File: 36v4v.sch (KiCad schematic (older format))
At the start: 38 parts, among them J1 Conn_01x03, J2 Conn_01x02, J3 Conn_01x02, J4 Conn_01x02, J5 Conn_01x02, U1 InnoSwitch3-CE, INN3162C, inS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

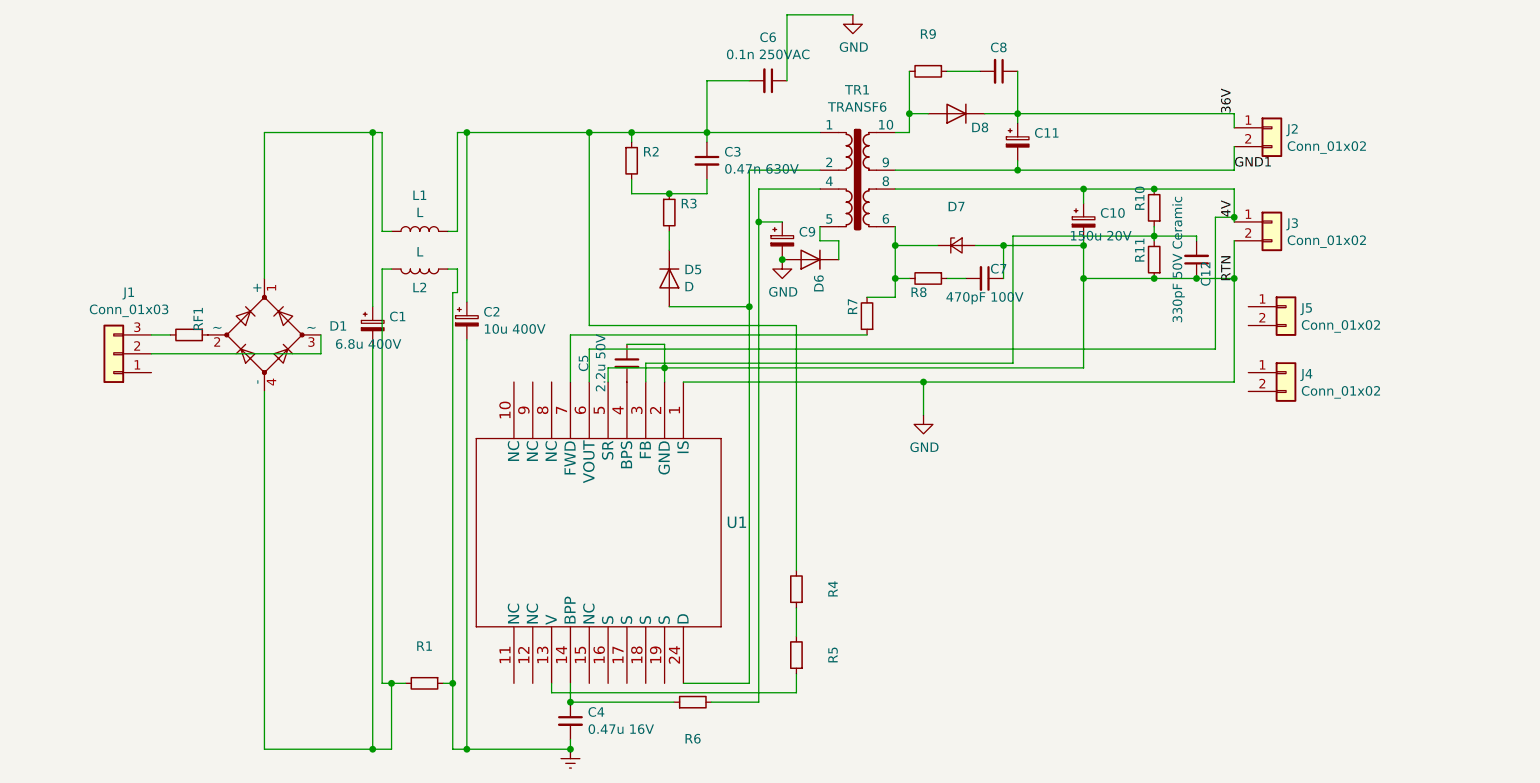
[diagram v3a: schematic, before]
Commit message: Changes to components and footprints as suggested by AA
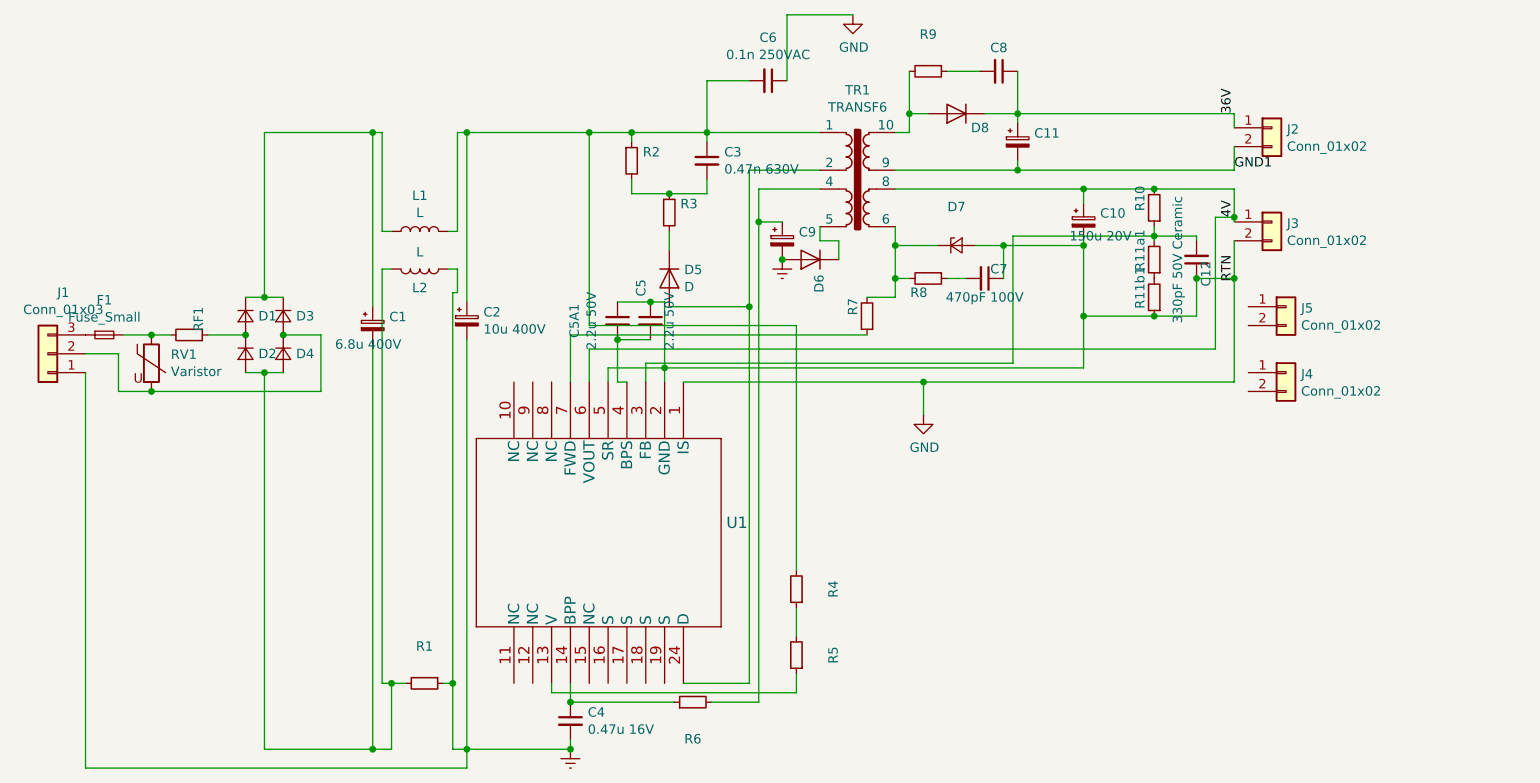
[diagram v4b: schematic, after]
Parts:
- removed D1: D_Bridge_+AA- / 800 V, 1 A, Standard Recovery, DO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, Diode_THT:Diode_Bridge_Vishay_GBL, symbol Device:D_Bridge_+AA-
- added C5A1: 2.2u 50V, Capacitor_SMD:C_0603_1608Metric_Pad1.05x0.95mm_HandSolder, symbol Device:C_Small
- added D1, D2, D3, D4: D_Small, Diode_SMD:D_SMB_Handsoldering, symbol Device:D_Small
- added F1: Fuse_Small, Fuse:Fuse_0805_2012Metric, symbol Device:Fuse_Small
- added R11b1: 29.4 kΩ, 1 %, 0.125 W, Metal Film, Resistor_SMD:R_0603_1608Metric_Pad1.05x0.95mm_HandSolder, symbol Device:R_Small
- added RV1: Varistor, Varistor:RV_Disc_D7mm_W4mm_P5mm, symbol Device:Varistor
- C1, C2: footprint pwrcon:CP_Elec_EEV_16x17.5 -> Capacitor_THT:CP_Radial_D10.0mm_P5.00mm; MFG Name Panasonic -> Kemet/Panasonic; MFG Part Num EEV-EB2G100SM -> ESH106M450AH4AA/EEV-EB2G100SM
- C10: MFG Name Nichikon -> Nichikon/Wurth; MFG Part Num PLF1D151MDO2TD -> PLF1D151MDO2TD/860010674014
- C11: MFG Name United Chemi-Con -> Wurth/United Chemi-Con; MFG Part Num EKZE500ELL220ME11D -> 860020672011/EKZE500ELL220ME11D
- C12: footprint Capacitor_THT:CP_Radial_D8.0mm_P5.00mm -> Capacitor_SMD:C_0603_1608Metric_Pad1.05x0.95mm_HandSolder; MFG Name Vishay -> Wurth/Vishay; MFG Part Num K471J15C0GH5TH5 -> 885342006005/K471J15C0GH5TH5
- C4: MFG Name TDK -> Murata/TDK; MFG Part Num FK18X7R1C474K -> GRM033R71E471KA01D/FK18X7R1C474K
- C5: MFG Name Kemet -> Murata/Kemet; MFG Part Num C340C225K5R5TA -> GRM188R61H225KE11D/C340C225K5R5TA
- C6: footprint Capacitor_SMD:C_0603_1608Metric_Pad1.05x0.95mm_HandSolder -> Capacitor_THT:C_Disc_D8.0mm_W5.0mm_P10.00mm
- C7: footprint Capacitor_THT:C_Disc_D8.0mm_W2.5mm_P5.00mm -> Capacitor_SMD:C_0603_1608Metric_Pad1.05x0.95mm_HandSolder; MFG Name Vishay -> Wurth/Vishay; MFG Part Num K471J15C0GH5TH5 -> 885342006005/K471J15C0GH5TH5
- C9: footprint Capacitor_THT:CP_Radial_D10.0mm_P5.00mm -> Capacitor_THT:CP_Radial_D5.0mm_P2.00mm; MFG Name Panasonic -> Wurth/Panasonic; MFG Part Num EEU-FC1V220H -> 860020672011/EEU-FC1V220H
- D5: footprint Diode_SMD:D_0603_1608Metric_Pad1.05x0.95mm_HandSolder -> Diode_SMD:D_SMA_Handsoldering; MFG Name (none) -> Vishay; MFG Part Num (none) -> US1M
- D6: footprint Diode_SMD:D_0603_1608Metric_Pad1.05x0.95mm_HandSolder -> Diode_SMD:D_SMA_Handsoldering; MFG Name ON Semi -> Vishay/ON Semi; MFG Part Num 1N3595TR -> US1M/1N3595TR
- D7: footprint Diode_SMD:D_0603_1608Metric_Pad1.05x0.95mm_HandSolder -> Diode_THT:D_DO-15_P10.16mm_Horizontal
- D8: footprint Diode_SMD:D_0603_1608Metric_Pad1.05x0.95mm_HandSolder -> Diode_SMD:D_SMA_Handsoldering; MFG Name Phillips -> Vishay/Phillips; MFG Part Num BYV26B-TR -> US1M/BYV26B-TR
- R1, R3, R4, R5, R6: footprint Resistor_SMD:R_0603_1608Metric_Pad1.05x0.95mm_HandSolder -> Resistor_SMD:R_0805_2012Metric_Pad1.15x1.40mm_HandSolder
- R2: footprint Resistor_SMD:R_0603_1608Metric_Pad1.05x0.95mm_HandSolder -> Resistor_SMD:R_2512_6332Metric_Pad1.52x3.35mm_HandSolder
- RF1: footprint Resistor_SMD:R_0603_1608Metric_Pad1.05x0.95mm_HandSolder -> Resistor_SMD:R_2816_7142Metric; MFG Name (none) -> TE Connectivity; MFG Part Num (none) -> SMW210RJT
- renumbered R11 to R11a1
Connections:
- net Earth: now also C9.2, D6.2 (A), J1.1 (Pin_1)
- net GND: now also C5A1.1, R11b1.1; no longer C9.2, D6.2 (A), R11a1.1
- net at C1.1, L1.1: now also D1.1 (K), D3.1 (K)
- net at C1.2, L2.2, R1.2: now also D2.2 (A), D4.2 (A)
- net at J1.2 (Pin_2): now also D3.2 (A), D4.1 (K), RV1.2
- net at J1.3 (Pin_3): now also F1.1; no longer RF1.2
- net at RF1.1: now also D1.2 (A), D2.1 (K)
- net at C5.2, U1.4 (BPS): now also C5A1.2
- new net: F1.2, RF1.2, RV1.1
- new net: R11a1.1, R11b1.2
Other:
- moved on the sheet: C5, J1

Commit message: More changes as per AA
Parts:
- added J6, J7: Conn_01x02, Connector_PinHeader_2.54mm:PinHeader_1x02_P2.54mm_Vertical, symbol Connector_Generic:Conn_01x02
- D7: footprint Diode_THT:D_DO-15_P10.16mm_Horizontal -> Diode_THT:D_DO-27_P5.08mm_Vertical_AnodeUp
- F1: footprint Fuse:Fuse_0805_2012Metric -> Fuse:Fuseholder_Cylinder-5x20mm_Schurter_0031_8201_Horizontal_Open
- renumbered C9 to C10, C10 to C11, C11 to C12, C12 to C13, C5A1 to C6, C6 to C7, C7 to C8, C8 to C9, R11a1 to R11, R11b1 to R12
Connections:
- net at F1.1, J1.3 (Pin_3): now also RV1.1
- net at F1.2, RF1.2: no longer RV1.1
- net at J4.1 (Pin_1): now also J7.2 (Pin_2)
- net at J4.2 (Pin_2): now also J7.1 (Pin_1)
- net at J5.1 (Pin_1): now also J6.2 (Pin_2)
- net at J5.2 (Pin_2): now also J6.1 (Pin_1)
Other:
- moved on the sheet: F1, J4, J5, RV1
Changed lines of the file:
@@
 Connection ~ 4975 1775
 $Comp
-L Device:C_Small C6
+L Device:C_Small C7
 U 1 1 5E48BA71
 P 5500 1175
-F 0 "C6" V 5271 1175 50  0000 C CNN
+F 0 "C7" V 5271 1175 50  0000 C CNN
 F 1 "0.1n 250VAC" V 5362 1175 50  0000 C CNN
 F 2 "Capacitor_THT:C_Disc_D8.0mm_W5.0mm_P10.00mm" H 5500 1175 50  0001 C CNN
@@
 $EndComp
 $Comp
-L Device:C_Small C8
+L Device:C_Small C9
 U 1 1 5E493F9C
 P 6725 1125
-F 0 "C8" V 6600 1125 50  0000 C CNN
+F 0 "C9" V 6600 1125 50  0000 C CNN
 F 1 "18pF 1KV Ceramic" V 6587 1125 50  0001 C CNN
 F 2 "Capacitor_THT:CP_Radial_D10.0mm_P5.00mm" H 6725 1125 50  0001 C CNN
@@
 $EndComp
 $Comp
-L Device:C_Small C7
+L Device:C_Small C8
 U 1 1 5E4944FB
 P 6650 2225
-F 0 "C7" V 6600 2300 50  0000 C CNN
+F 0 "C8" V 6600 2300 50  0000 C CNN
 F 1 "470pF 100V" V 6750 2225 50  0000 C CNN
 F 2 "Capacitor_SMD:C_0603_1608Metric_Pad1.05x0.95mm_HandSolder" H 6650 2225 50  0001 C CNN
@@
 	6450 1125 6625 1125
 $Comp
-L Device:CP_Small C11
+L Device:CP_Small C12
 U 1 1 5E4AE12A
 P 6825 1500
-F 0 "C11" H 6913 1546 50  0000 L CNN
+F 0 "C12" H 6913 1546 50  0000 L CNN
 F 1 "22u 50V Electrolytic" H 6913 1455 50  0001 L CNN
 F 2 "Capacitor_THT:CP_Radial_D5.0mm_P2.00mm" H 6825 1500 50  0001 C CNN
@@
 Connection ~ 6825 1350
 $Comp
-L Device:CP_Small C10
+L Device:CP_Small C11
 U 1 1 5E4C1814
 P 7175 1925
-F 0 "C10" H 7263 1971 50  0000 L CNN
+F 0 "C11" H 7263 1971 50  0000 L CNN
 F 1 "150u 20V" H 7100 1850 50  0000 L CNN
 F 2 "Capacitor_THT:CP_Radial_D10.0mm_P5.00mm" H 7175 1925 50  0001 C CNN
@@
 	5450 4475 5450 1925
 $Comp
-L Device:CP_Small C9
+L Device:CP_Small C10
 U 1 1 5E68E711
 P 5575 2025
-F 0 "C9" H 5663 2071 50  0000 L CNN
+F 0 "C10" H 5663 2071 50  0000 L CNN
 F 1 "22u 35V Electrolytic" H 5663 1980 50  0001 L CNN
 F 2 "Capacitor_THT:CP_Radial_D5.0mm_P2.00mm" H 5575 2025 50  0001 C CNN
@@
 F 0 "D7" H 6500 2255 50  0000 C CNN
 F 1 "40 V, 2 A, Schottky, DO-15" H 6500 2164 50  0001 C CNN
-F 2 "Diode_THT:D_DO-15_P10.16mm_Horizontal" V 6500 2050 50  0001 C CNN
+F 2 "Diode_THT:D_DO-27_P5.08mm_Vertical_AnodeUp" V 6500 2050 50  0001 C CNN
 F 3 "~" V 6500 2050 50  0001 C CNN
 F 4 "Vishay" H 6500 2050 50  0001 C CNN "MFG Name"
@@
 Connection ~ 7175 1750
 $Comp
-L Device:R_Small R11a1
+L Device:R_Small R11
 U 1 1 5E716C35
 P 7550 2125
-F 0 "R11a1" V 7625 2075 50  0000 C CNN
+F 0 "R11" V 7625 2075 50  0000 C CNN
 F 1 "29.4 kΩ, 1 %, 0.125 W, Metal Film" V 7445 2125 50  0001 C CNN
 F 2 "Resistor_SMD:R_0603_1608Metric_Pad1.05x0.95mm_HandSolder" H 7550 2125 50  0001 C CNN
@@
 $EndComp
 $Comp
-L Device:C_Small C12
+L Device:C_Small C13
 U 1 1 5E8C030C
 P 7775 2125
-F 0 "C12" V 7725 2200 50  0000 C CNN
+F 0 "C13" V 7725 2200 50  0000 C CNN
 F 1 "330pF 50V Ceramic" V 7875 2125 50  0000 C CNN
 F 2 "Capacitor_SMD:C_0603_1608Metric_Pad1.05x0.95mm_HandSolder" H 7775 2125 50  0001 C CNN
@@
 L Connector_Generic:Conn_01x02 J4
 U 1 1 5E906E27
-P 8250 2725
-F 0 "J4" H 8330 2717 50  0000 L CNN
-F 1 "Conn_01x02" H 8330 2626 50  0000 L CNN
-F 2 "Connector_Wire:SolderWirePad_1x02_P5.08mm_Drill1.5mm" H 8250 2725 50  0001 C CNN
-F 3 "~" H 8250 2725 50  0001 C CNN
-	1    8250 2725
-	1    0    0    -1
+P 8500 3100
+F 0 "J4" H 8580 3092 50  0000 L CNN
+F 1 "Conn_01x02" H 8580 3001 50  0000 L CNN
+F 2 "Connector_Wire:SolderWirePad_1x02_P5.08mm_Drill1.5mm" H 8500 3100 50  0001 C CNN
+F 3 "~" H 8500 3100 50  0001 C CNN
+	1    8500 3100
+	-1   0    0    1
 $EndComp
 $Comp
 L Connector_Generic:Conn_01x02 J5
 U 1 1 5E909967
-P 8250 2375
-F 0 "J5" H 8330 2367 50  0000 L CNN
-F 1 "Conn_01x02" H 8330 2276 50  0000 L CNN
-F 2 "Connector_Wire:SolderWirePad_1x02_P5.08mm_Drill1.5mm" H 8250 2375 50  0001 C CNN
-F 3 "~" H 8250 2375 50  0001 C CNN
-	1    8250 2375
-	1    0    0    -1
+P 8525 2325
+F 0 "J5" H 8605 2317 50  0000 L CNN
+F 1 "Conn_01x02" H 8605 2226 50  0000 L CNN
+F 2 "Connector_Wire:SolderWirePad_1x02_P5.08mm_Drill1.5mm" H 8525 2325 50  0001 C CNN
+F 3 "~" H 8525 2325 50  0001 C CNN
+	1    8525 2325
+	-1   0    0    1
 $EndComp
 Wire Wire Line
@@
 	7175 2050 7175 2425
 $Comp
-L Device:R_Small R11b1
+L Device:R_Small R12
 U 1 1 5E9AEDCF
 P 7550 2325
-F 0 "R11b1" V 7625 2275 50  0000 C CNN
+F 0 "R12" V 7625 2275 50  0000 C CNN
 F 1 "29.4 kΩ, 1 %, 0.125 W, Metal Film" V 7445 2325 50  0001 C CNN
 F 2 "Resistor_SMD:R_0603_1608Metric_Pad1.05x0.95mm_HandSolder" H 7550 2325 50  0001 C CNN
@@
 Connection ~ 7550 2425
 $Comp
-L Device:C_Small C5A1
+L Device:C_Small C6
 U 1 1 5E9E2EF2
 P 4700 2450
-F 0 "C5A1" V 4471 2450 50  0000 C CNN
+F 0 "C6" V 4471 2450 50  0000 C CNN
 F 1 "2.2u 50V" V 4562 2450 50  0000 C CNN
 F 2 "Capacitor_SMD:C_0603_1608Metric_Pad1.05x0.95mm_HandSolder" H 4700 2450 50  0001 C CNN
@@
 $EndComp
 Connection ~ 5575 2125
-Wire Wire Line
-	2075 2525 2225 2525
 $Comp
 L Device:Fuse_Small F1
 U 1 1 5EAD9C99
-P 1975 2525
-F 0 "F1" H 1975 2710 50  0000 C CNN
-F 1 "Fuse_Small" H 1975 2619 50  0000 C CNN
-F 2 "Fuse:Fuse_0805_2012Metric" H 1975 2525 50  0001 C CNN
-F 3 "~" H 1975 2525 50  0001 C CNN
-	1    1975 2525
+P 2175 2525
+F 0 "F1" H 2175 2710 50  0000 C CNN
+F 1 "Fuse_Small" H 2175 2619 50  0000 C CNN
+F 2 "Fuse:Fuseholder_Cylinder-5x20mm_Schurter_0031_8201_Horizontal_Open" H 2175 2525 50  0001 C CNN
+F 3 "~" H 2175 2525 50  0001 C CNN
+	1    2175 2525
 	1    0    0    -1
 $EndComp
@@
 L Device:Varistor RV1
 U 1 1 5EAE8BC1
-P 2225 2675
-F 0 "RV1" H 2328 2721 50  0000 L CNN
-F 1 "Varistor" H 2328 2630 50  0000 L CNN
-F 2 "Varistor:RV_Disc_D7mm_W4mm_P5mm" V 2155 2675 50  0001 C CNN
-F 3 "~" H 2225 2675 50  0001 C CNN
-	1    2225 2675
-	1    0    0    -1
-$EndComp
-Connection ~ 2225 2525
-Wire Wire Line
-	2225 2525 2325 2525
-Wire Wire Line
-	1875 2625 2050 2625
-Wire Wire Line
-	2050 2625 2050 2825
-Wire Wire Line
-	2050 2825 2225 2825
-Wire Wire Line
-	2225 2825 3125 2825
+P 2075 2675
+F 0 "RV1" H 2178 2721 50  0000 L CNN
+F 1 "Varistor" H 2178 2630 50  0000 L CNN
+F 2 "Varistor:RV_Disc_D7mm_W4mm_P5mm" V 2005 2675 50  0001 C CNN
+F 3 "~" H 2075 2675 50  0001 C CNN
+	1    2075 2675
+	1    0    0    -1
+$EndComp
 Wire Wire Line
 	3125 2525 3125 2825
-Connection ~ 2225 2825
 Wire Wire Line
 	1875 2725 1875 4825
 Wire Wire Line
 	1875 4825 3900 4825
+Wire Wire Line
+	2075 2825 3125 2825
+Wire Wire Line
+	2275 2525 2325 2525
+Wire Wire Line
+	1875 2625 1950 2625
+Wire Wire Line
+	1950 2625 1950 2825
+Wire Wire Line
+	1875 2525 2075 2525
+Connection ~ 2075 2525
+Wire Wire Line
+	1950 2825 2075 2825
+Connection ~ 2075 2825
+$Comp
+L Connector_Generic:Conn_01x02 J6
+U 1 1 5E967EA6
+P 8925 2225
+F 0 "J6" H 9005 2217 50  0000 L CNN
+F 1 "Conn_01x02" H 9005 2126 50  0000 L CNN
+F 2 "Connector_PinHeader_2.54mm:PinHeader_1x02_P2.54mm_Vertical" H 8925 2225 50  0001 C CNN
+F 3 "~" H 8925 2225 50  0001 C CNN
+	1    8925 2225
+	1    0    0    -1
+$EndComp
+$Comp
+L Connector_Generic:Conn_01x02 J7
+U 1 1 5E9687B5
+P 8900 3000
+F 0 "J7" H 8980 2992 50  0000 L CNN
+F 1 "Conn_01x02" H 8980 2901 50  0000 L CNN
+F 2 "Connector_PinHeader_2.54mm:PinHeader_1x02_P2.54mm_Vertical" H 8900 3000 50  0001 C CNN
+F 3 "~" H 8900 3000 50  0001 C CNN
+	1    8900 3000
+	1    0    0    -1
+$EndComp
 $EndSCHEMATC

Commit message: Diode footprint change
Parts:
- D7: footprint Diode_THT:D_DO-27_P5.08mm_Vertical_AnodeUp -> Diode_SMD:D_SMA_Handsoldering; MFG Part Num SB240-E3/54 -> B240A-E3/61T OR SB240-E3/54
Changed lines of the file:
@@
 F 0 "D7" H 6500 2255 50  0000 C CNN
 F 1 "40 V, 2 A, Schottky, DO-15" H 6500 2164 50  0001 C CNN
-F 2 "Diode_THT:D_DO-27_P5.08mm_Vertical_AnodeUp" V 6500 2050 50  0001 C CNN
+F 2 "Diode_SMD:D_SMA_Handsoldering" V 6500 2050 50  0001 C CNN
 F 3 "~" V 6500 2050 50  0001 C CNN
 F 4 "Vishay" H 6500 2050 50  0001 C CNN "MFG Name"
-F 5 "SB240-E3/54 " H 6500 2050 50  0001 C CNN "MFG Part Num"
+F 5 "B240A-E3/61T OR SB240-E3/54 " H 6500 2050 50  0001 C CNN "MFG Part Num"
 	1    6500 2050
 	1    0    0    -1
